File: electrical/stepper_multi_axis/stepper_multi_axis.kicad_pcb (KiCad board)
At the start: 4 copper layers, 152.4 x 69.8 mm, 71 parts, among them J1 Conn_01x04_Male, J10 Conn_01x02_Male, J11 Conn_01x01_Male, J12 Conn_01x01_Male, J13 Conn_01x06, J14 Conn_01x01_Male, J15 Conn_01x01_Male, J16 Conn_01x01_Male, J17 Conn_01x01_Male, J18 Conn_01x01_Male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

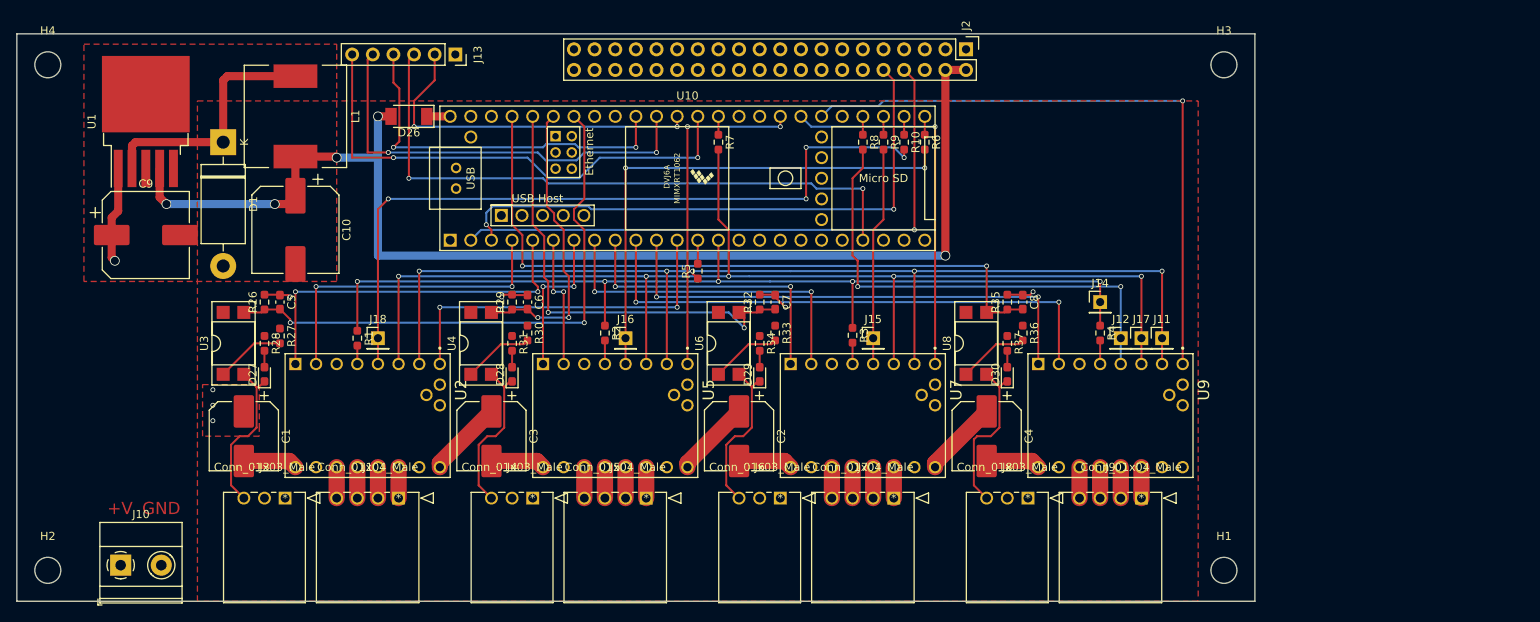
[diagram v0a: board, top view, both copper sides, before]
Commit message: added higher current drivers
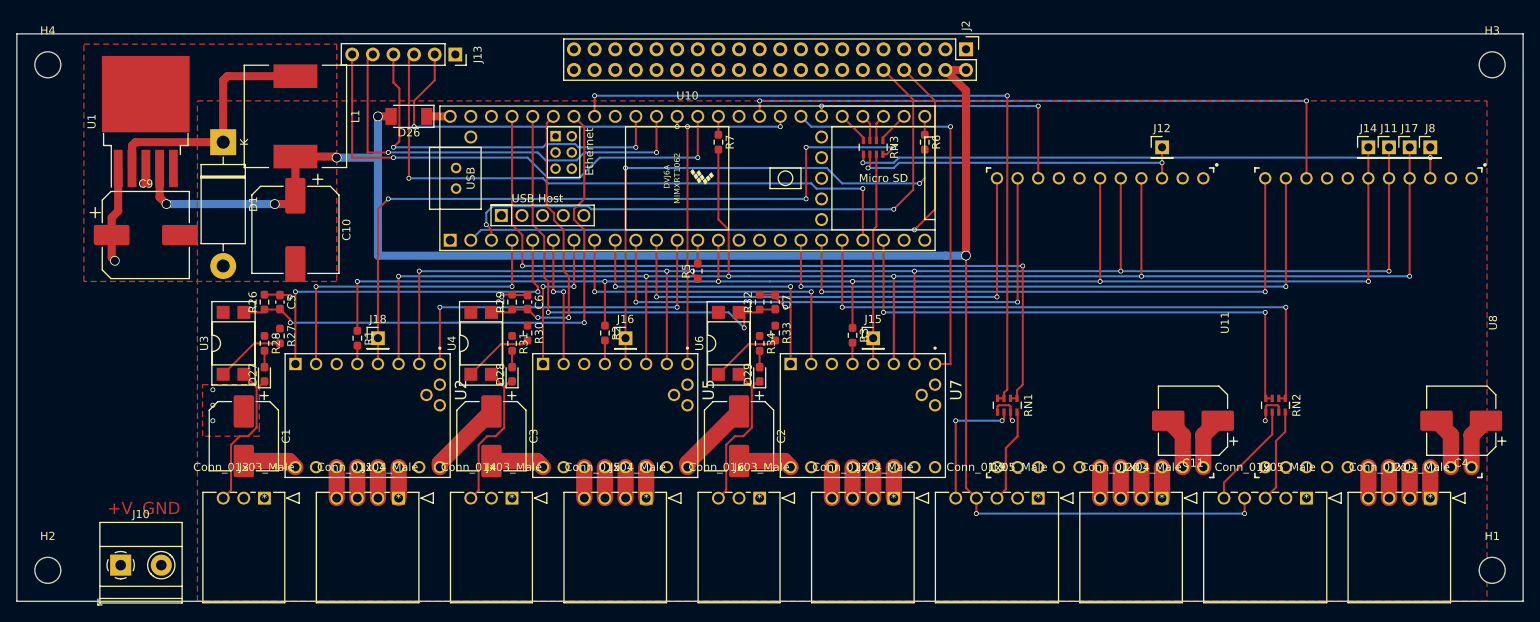
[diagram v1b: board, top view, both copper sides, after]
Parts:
- removed C8: 100nF, Capacitor_SMD:C_0603_1608Metric_Pad1.08x0.95mm_HandSolder
- removed D30: LED, LED_SMD:LED_0603_1608Metric_Pad1.05x0.95mm_HandSolder
- removed R10, R35, R36, R37, R4, R8, R9: 100, Resistor_SMD:R_0603_1608Metric_Pad0.98x0.95mm_HandSolder
- removed U9: TMC5160_SILENTSTEPSTICK, Trinamic:MODULE_TMC_SILENTSTEPSTICK
- added C11: 10uF, Capacitor_SMD:CP_Elec_8x6.7, F.Cu at (218.4, 128.9)
- added J19: Conn_01x05_Male, sl_connector:1719740105, F.Cu at (199.4, 138.4)
- added J20: Conn_01x04_Male, sl_connector:1719740104, F.Cu at (214.6, 138.4)
- added J21: Conn_01x04_Male, sl_connector:1719740104, F.Cu at (247.7, 138.4)
- added RN1: R_Pack04, Resistor_SMD:R_Array_Concave_4x0603, F.Cu at (195.6, 127.0)
- added RN2: R_Pack04, Resistor_SMD:R_Array_Concave_4x0603, F.Cu at (228.6, 127.0)
- added RN3: R_Pack04, Resistor_SMD:R_Array_Concave_4x0603, F.Cu at (179.1, 95.2)
- added U11: TMC5160-BOB, trinamic-footprints:22pin1,5x1,1-BOB, F.Cu at (207.0, 116.8)
- J8: value Conn_01x03_Male -> Conn_01x01_Male; footprint sl_connector:1719740103 -> Connector_PinHeader_2.54mm:PinHeader_1x01_P2.54mm_Vertical
- J9: value Conn_01x04_Male -> Conn_01x05_Male; footprint sl_connector:1719740104 -> sl_connector:1719740105
- U8: value LTV-817 -> TMC5160-BOB; footprint Package_DIP:DIP-4_W7.62mm_SMDSocket_SmallPads -> trinamic-footprints:22pin1,5x1,1-BOB
- moved J8 65.7 mm to (247.7, 95.2)
- moved C4 58.5 mm to (251.5, 128.9), turned to 180 degrees
- moved U8 48.3 mm to (240.0, 116.8), turned to 270 degrees
- moved J17 40.5 mm to (245.1, 95.2)
- moved J14 38.1 mm to (240.0, 95.2)
- moved J11 36.5 mm to (242.6, 95.2)
- moved H1 33.0 mm to (255.3, 147.3)
- moved H3 33.0 mm to (255.3, 85.1)
- moved J12 24.0 mm to (214.6, 95.2)
- moved J9 20.3 mm to (232.4, 138.4)
- moved J3 2.54 mm to (104.1, 138.4)
- moved J4 2.54 mm to (134.6, 138.4)
- moved J6 2.54 mm to (165.1, 138.4)
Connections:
- net /Stepper_Driver_X/CS renamed /CS_X
- net /sheet608DFF62/CS renamed /CS_Y
- net /sheet608FE262/CS renamed /CS_Z
- net /sheet608FE262/Limit renamed /LIM_Z
- J11 pad 1: /Stepper_Driver_X/SDI -> /MOSI
- J12 pad 1: /sheet608FE263/CS -> /CS_A
- J14 pad 1: /Stepper_Driver_X/SDO -> /MISO
- J17 pad 1: /Stepper_Driver_X/SCK -> /SCK
- J8 pad 1: +3V3 -> /CS_B
- J9 pad 1: Net-(J9-Pad1) -> GND
- J9 pad 4: Net-(J9-Pad4) -> +5V
- R1 pad 1: /Stepper_Driver_X/SDO -> /MISO
- R2 pad 1: /Stepper_Driver_X/SDO -> /MISO
- R3 pad 1: /Stepper_Driver_X/SDO -> /MISO
- R5 pad 1: /Stepper_Driver_X/SDI -> /MOSI
- R7 pad 2: /Stepper_Driver_X/SCK -> /SCK
- U10 pad 10: /RPi_GPIO/A_STEP -> /ST_A
- U10 pad 11: /RPi_GPIO/A_DIR -> /D_A
- U10 pad 14: /Stepper_Driver_X/SDO -> /MISO
- U10 pad 18: /RPi_GPIO/B_STEP -> /ST_B
- U10 pad 19: /RPi_GPIO/B_DIR -> /D_B
- U10 pad 20: /RPi_GPIO/B_LIMIT -> /ENCA_B
- U10 pad 22: Net-(U10-Pad22) -> /ENCB_B
- U10 pad 29: /RPi_GPIO/B_ENABLE -> Net-(RN3-Pad4)
- U10 pad 30: /RPi_GPIO/A_ENABLE -> /EN_A
- U10 pad 33: Net-(U10-Pad33) -> /EN_B
- U10 pad 41: /RPi_GPIO/COOLANT_FLOOD -> /ENCB_A
- U10 pad 45: /RPi_GPIO/A_LIMIT -> /ENCA_A
- U2 pad JP1_6: /Stepper_Driver_X/SCK -> /SCK
- U2 pad JP1_7: /Stepper_Driver_X/SDI -> /MOSI
- U5 pad JP1_6: /Stepper_Driver_X/SCK -> /SCK
- U5 pad JP1_7: /Stepper_Driver_X/SDI -> /MOSI
- U7 pad JP1_6: /Stepper_Driver_X/SCK -> /SCK
- U7 pad JP1_7: /Stepper_Driver_X/SDI -> /MOSI
- U8 pad 1: Net-(R36-Pad2) -> +3V3
- U8 pad 2: Net-(D30-Pad1) -> GND
- U8 pad 3: /RPi_GPIO/A_LIMIT -> /CS_B
- U8 pad 4: +3V3 -> /SCK
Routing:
- net /SCK: track 0.00 -> 200.9 mm, vias 0 -> 6
- net /MOSI: track 0.00 -> 181.5 mm, vias 0 -> 6
- net /MISO: track 0.00 -> 176.0 mm, vias 0 -> 6
- net /Stepper_Driver_X/SCK: track 150.7 -> 0.00 mm, vias 5 -> 0
- net /Stepper_Driver_X/SDI: track 138.3 -> 0.00 mm, vias 5 -> 0
- net /Stepper_Driver_X/SDO: track 119.2 -> 0.00 mm, vias 5 -> 0
- net /ENCA_A: track 0.00 -> 97.9 mm, vias 0 -> 2
- net /ENCB_A: track 0.00 -> 91.6 mm, vias 0 -> 2
- net /RPi_GPIO/A_LIMIT: track 86.4 -> 0.00 mm, vias 2 -> 0
- net /EN_B: track 0.00 -> 78.7 mm, vias 0 -> 2
- net /ST_B: track 0.00 -> 78.7 mm, vias 0 -> 2
- net /RPi_GPIO/A_ENABLE: track 77.6 -> 0.00 mm, vias 1 -> 0
- net /CS_B: track 0.00 -> 75.0 mm, vias 0 -> 2
- net /D_B: track 0.00 -> 74.9 mm, vias 0 -> 2
- net /ENCA_B: track 0.00 -> 74.9 mm, vias 0 -> 2
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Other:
- board size 152.4 x 69.8 mm -> 185.4 x 69.8 mm

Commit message: shipped things
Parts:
- added C12: 100nF, Capacitor_SMD:C_0603_1608Metric_Pad1.08x0.95mm_HandSolder, F.Cu at (74.9, 44.5)
- added C13: 100nF, Capacitor_SMD:C_0603_1608Metric_Pad1.08x0.95mm_HandSolder, F.Cu at (89.5, 40.5)
- added C8: 100nF, Capacitor_SMD:C_0603_1608Metric_Pad1.08x0.95mm_HandSolder, F.Cu at (67.8, 34.7)
- added D2: LED, Diode_SMD:D_0603_1608Metric_Pad1.05x0.95mm_HandSolder, F.Cu at (39.3, 79.7)
- added J22: Conn_01x02_Male, Connector_PinHeader_2.54mm:PinHeader_1x02_P2.54mm_Vertical, F.Cu at (52.5, 78.9)
- added J23: Conn_01x01, Connector_PinHeader_2.54mm:PinHeader_1x01_P2.54mm_Vertical, F.Cu at (61.5, 78.7)
- added J24: Conn_01x01, Connector_PinHeader_2.54mm:PinHeader_1x01_P2.54mm_Vertical, F.Cu at (58.0, 68.3)
- added J25: Conn_01x01, Connector_PinHeader_2.54mm:PinHeader_1x01_P2.54mm_Vertical, F.Cu at (65.5, 68.3)
- added J26: Conn_01x01, Connector_PinHeader_2.54mm:PinHeader_1x01_P2.54mm_Vertical, F.Cu at (55.8, 44.5)
- added J27: Conn_01x01, Connector_PinHeader_2.54mm:PinHeader_1x01_P2.54mm_Vertical, F.Cu at (57.8, 78.7)
- added J28: Conn_01x01, Connector_PinHeader_2.54mm:PinHeader_1x01_P2.54mm_Vertical, F.Cu at (46.4, 68.3)
- added J29: Conn_01x01, Connector_PinHeader_2.54mm:PinHeader_1x01_P2.54mm_Vertical, F.Cu at (50.4, 68.3)
- added J30: Conn_01x01, Connector_PinHeader_2.54mm:PinHeader_1x01_P2.54mm_Vertical, F.Cu at (54.1, 68.3)
- added J31: HDMI_A_1.4, HDMI:TE_1827059-3, F.Cu at (57.3, 29.5)
- added J32: USB_A, Connector_USB:USB_A_Molex_67643_Horizontal, F.Cu at (88.7, 36.4)
- added R4: 1k, Resistor_SMD:R_0603_1608Metric_Pad0.98x0.95mm_HandSolder, F.Cu at (43.0, 79.7)
- added R8: 2.2k, Resistor_SMD:R_0603_1608Metric_Pad0.98x0.95mm_HandSolder, F.Cu at (80.3, 41.2)
- added R9: 2.2k, Resistor_SMD:R_0603_1608Metric_Pad0.98x0.95mm_HandSolder, F.Cu at (80.3, 44.5)
- added U12: FSUSB42MUX, usbmux:SOP50P490X110-10N, F.Cu at (77.5, 43.3)
- added U9: Compute_Module_4_Connectors, RPi_Compute_Module_4:Raspberry-Pi-4-Compute-Module, F.Cu at (49.8, 56.7)
- D1: value 1N5822 -> D_Schottky; footprint Diode_THT:D_DO-201AD_P15.24mm_Horizontal -> Diode_SMD:D_SOD-128
- J13: value Conn_01x06 -> USB_B_Micro; footprint Connector_PinSocket_2.54mm:PinSocket_1x06_P2.54mm_Vertical -> Connector_USB:USB_Micro-B_Molex-105017-0001
- J2: value RPi_GPIO -> Conn_01x01; footprint RPi_Hat:Pin_Header_Straight_2x20 -> Connector_PinHeader_2.54mm:PinHeader_1x01_P2.54mm_Vertical
- RN1, RN2: value R_Pack04 -> R_1K_4
- RN3: value R_Pack04 -> R_100_4
- U3, U4, U6: footprint Package_DIP:DIP-4_W7.62mm_SMDSocket_SmallPads -> Package_DIP:DIP-4_W8.89mm_SMDSocket_LongPads
- moved H1 263.0 mm to (21.6, 26.7), turned to 180 degrees
- moved H3 233.7 mm to (21.6, 88.9), turned to 180 degrees
- moved H2 227.6 mm to (270.5, 26.7), turned to 180 degrees
- moved J10 211.2 mm to (261.5, 28.6), turned to 180 degrees
- moved H4 193.1 mm to (270.5, 88.9), turned to 180 degrees
- moved J21 179.0 mm to (100.3, 36.8), turned to 180 degrees
- moved C4 175.6 mm to (96.5, 46.4), turned to 0 degrees
- moved C9 172.9 mm to (258.4, 69.2), turned to 180 degrees
- moved J3 172.7 mm to (243.8, 36.8), turned to 180 degrees
- moved U1 169.1 mm to (258.4, 83.2), turned to 270 degrees
- moved C1 168.6 mm to (246.4, 44.5), turned to 90 degrees
- moved U3 160.2 mm to (247.7, 56.5), turned to 270 degrees
- moved D27 156.8 mm to (243.8, 52.1), turned to 270 degrees
- moved J9 154.8 mm to (115.6, 36.8), turned to 180 degrees
- moved R28 153.5 mm to (243.8, 55.9), turned to 90 degrees
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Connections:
- J13 pad 1: GND -> Net-(J13-Pad1)
- J13 pad 2: /RPi_GPIO/PROBE -> /Sheet614CFDB6/PROG-
- J13 pad 3: /RPi_GPIO/SAFETY_DOOR -> /Sheet614CFDB6/PROG+
- J13 pad 4: /RPi_GPIO/CYCLE_START -> Net-(J13-Pad4)
- J13 pad 5: /RPi_GPIO/FEED_HOLD -> GND
- J13 pad 6: /RPi_GPIO/CNC_RESET -> GND
- J2 pad 1: Net-(J2-Pad1) -> /Sheet613FBD85/USB_OTG
- U10 pad 2: /RPi_GPIO/PI_TX -> Net-(U10-Pad2)
- U10 pad 3: /RPi_GPIO/PI_RX -> Net-(U10-Pad3)
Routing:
- net +5V: track 220.9 -> 332.4 mm, vias 7 -> 8
- net /RPi_GPIO/SAFETY_DOOR: track 78.3 -> 0.00 mm, vias 2 -> 0
- net /RPi_GPIO/PI_TX: track 77.5 -> 0.00 mm, vias 1 -> 0
- net /RPi_GPIO/PI_RX: track 73.9 -> 0.00 mm, vias 2 -> 0
- net +3.3VA: track 0.00 -> 73.7 mm, vias 0 -> 1
- net /RPi_GPIO/CNC_RESET: track 62.4 -> 0.00 mm, vias 2 -> 0
- net /Sheet613FBD85/USB_OTG: track 0.00 -> 57.0 mm, vias 0 -> 2
- net /RPi_GPIO/FEED_HOLD: track 53.1 -> 0.00 mm, vias 2 -> 0
- net /RPi_GPIO/CYCLE_START: track 46.0 -> 0.00 mm, vias 2 -> 0
- net /RPi_GPIO/PROBE: track 43.6 -> 0.00 mm, vias 2 -> 0
- net /Sheet613FBD85/USB_N: track 0.00 -> 43.5 mm
- net /Sheet613FBD85/USB_P: track 0.00 -> 43.5 mm
- net GND: track 59.1 -> 81.6 mm, vias 5 -> 19
- net /Sheet613FBD85/HDMI0_HOTPLUG: track 0.00 -> 21.2 mm, vias 0 -> 2
- net /Sheet613FBD85/HDMI0_CEC: track 0.00 -> 17.3 mm, vias 0 -> 2
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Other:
- board size 185.4 x 69.8 mm -> 256.5 x 71.1 mm

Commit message: made some changes?
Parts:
- moved H1 95.6 mm to (3.81, -67.3)
- moved H2 95.6 mm to (252.7, -67.3)
- moved C1 94.4 mm to (228.6, -48.3)
- moved C10 94.4 mm to (225.4, -23.5)
- moved C12 94.4 mm to (57.1, -48.3)
- moved C13 94.4 mm to (71.8, -52.2)
- moved C2 94.4 mm to (167.6, -48.3)
- moved C3 94.4 mm to (198.1, -48.3)
- moved C5 94.4 mm to (224.2, -31.8)
- moved C6 94.4 mm to (193.7, -31.8)
- moved C7 94.4 mm to (163.2, -31.8)
- moved C8 94.4 mm to (50.0, -58.0)
- moved C9 94.4 mm to (240.7, -23.5)
- moved D1 94.4 mm to (233.0, -16.5)
- moved D2 94.4 mm to (21.5, -13.0)
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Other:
- outline, holes or cut-outs redrawn

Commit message: pre delete thru hole
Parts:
- removed H2, H3, H4: MountingHole, MountingHole:MountingHole_3.2mm_M3
- added C14: 100nF, Capacitor_SMD:C_0603_1608Metric_Pad1.08x0.95mm_HandSolder, F.Cu at (139.3, 45.3)
- added C15: 100nF, Capacitor_SMD:C_0603_1608Metric_Pad1.08x0.95mm_HandSolder, F.Cu at (120.9, 45.3)
- added C16: 10uF, Capacitor_SMD:C_0603_1608Metric_Pad1.08x0.95mm_HandSolder, F.Cu at (158.2, 31.5)
- added C17: 10uF, Capacitor_SMD:C_0603_1608Metric_Pad1.08x0.95mm_HandSolder, F.Cu at (162.2, 31.4)
- added C18: 10uF, Capacitor_SMD:C_0603_1608Metric_Pad1.08x0.95mm_HandSolder, F.Cu at (167.5, 40.3)
- added C19: 100nF, Capacitor_SMD:C_0603_1608Metric_Pad1.08x0.95mm_HandSolder, F.Cu at (179.3, 38.4)
- added J33: USB_A, Connector_USB:USB_A_Molex_67643_Horizontal, F.Cu at (145.0, 46.6)
- added J34: USB_A, Connector_USB:USB_A_Molex_67643_Horizontal, F.Cu at (126.6, 46.6)
- added J35: MICROMOD-2222-C, SparkFun-MicroMod:M.2-CONNECTOR-E, F.Cu at (163.4, 20.6)
- added J36: Conn_01x02_Male, Connector_PinHeader_2.54mm:PinHeader_1x02_P2.54mm_Vertical, F.Cu at (177.3, 20.1)
- added J37: Conn_01x02_Male, Connector_PinHeader_2.54mm:PinHeader_1x02_P2.54mm_Vertical, F.Cu at (177.3, 23.6)
- added J39: USB_B_Micro, Connector_USB:USB_Micro-B_Molex-105017-0001, F.Cu at (180.0, 56.2)
- added R10: 2.7k, Resistor_SMD:R_0603_1608Metric_Pad0.98x0.95mm_HandSolder, F.Cu at (170.4, 40.9)
- added R11: 2.2k, Resistor_SMD:R_0603_1608Metric_Pad0.98x0.95mm_HandSolder, F.Cu at (178.1, 51.1)
- added R12: 2.2k, Resistor_SMD:R_0603_1608Metric_Pad0.98x0.95mm_HandSolder, F.Cu at (179.3, 36.4)
- added R13: 100, Resistor_SMD:R_0603_1608Metric_Pad0.98x0.95mm_HandSolder, F.Cu at (271.3, 0.51)
- added R14: 100, Resistor_SMD:R_0603_1608Metric_Pad0.98x0.95mm_HandSolder, F.Cu at (271.3, 3.02)
- added R15: 100, Resistor_SMD:R_0603_1608Metric_Pad0.98x0.95mm_HandSolder, F.Cu at (275.6, 0.51)
- added RN4: R_100_4, Resistor_SMD:R_Array_Concave_4x0603, F.Cu at (157.2, 14.0)
- added U13: FE1.1s, Package_SO:SSOP-28_3.9x9.9mm_P0.635mm, F.Cu at (163.8, 35.8)
- added U14: FSUSB42MUX, usbmux:SOP50P490X110-10N, F.Cu at (173.8, 35.8)
- added Y1: Crystal, Crystal:Crystal_HC50_Vertical, F.Cu at (153.9, 39.0)
- moved J13 182.1 mm to (189.4, 56.2), turned to 0 degrees
- moved H1 177.1 mm to (167.4, 0.32)
- moved R8 160.2 mm to (185.0, 51.7), turned to 180 degrees
- moved J2 154.0 mm to (181.6, 51.6), turned to 180 degrees
- moved J32 138.4 mm to (163.4, 46.6), turned to 0 degrees
- moved J31 137.1 mm to (111.9, 53.3), turned to 0 degrees
- moved U12 134.2 mm to (167.9, 30.1), turned to 0 degrees
- moved C12 130.8 mm to (162.8, 28.8), turned to 180 degrees
- moved C13 130.0 mm to (157.7, 45.3), turned to 180 degrees
- moved R9 123.0 mm to (158.4, 28.8), turned to 180 degrees
- moved C8 117.9 mm to (101.4, 48.1), turned to 270 degrees
- moved J26 111.1 mm to (113.4, 33.3), turned to 180 degrees
- moved D2 109.0 mm to (129.9, -1.95), turned to 0 degrees
- moved U9 104.4 mm to (119.4, 21.0), turned to 270 degrees
- moved R4 101.5 mm to (126.1, -1.95), turned to 180 degrees
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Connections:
- J32 pad 2: /Sheet614CFDB6/USB_A- -> /Sheet614CFDB6/1-
- J32 pad 3: /Sheet614CFDB6/USB_A+ -> /Sheet614CFDB6/1+
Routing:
- net /Sheet614CFDB6/3+: track 0.00 -> 39.8 mm
- net /Sheet614CFDB6/3-: track 0.00 -> 39.8 mm
- net +5V: track 332.4 -> 369.0 mm, vias 8 -> 9
- net +3.3VA: track 73.7 -> 42.8 mm, vias 1 -> 5
- net /Sheet614CFDB6/OVERRIDE-: track 0.00 -> 24.8 mm
- net /Sheet614CFDB6/OVERRIDE+: track 0.00 -> 24.1 mm
- net /Sheet614CFDB6/2-: track 0.00 -> 23.7 mm
- net /Sheet614CFDB6/2+: track 0.00 -> 23.7 mm
- net GND: track 81.6 -> 103.6 mm, vias 19 -> 31
- net Net-(R11-Pad2): track 0.00 -> 19.9 mm, vias 0 -> 2
- net /Sheet614CFDB6/PROG+: track 15.0 -> 34.8 mm
- net /Sheet614CFDB6/PROG-: track 15.0 -> 34.1 mm
- net Net-(C17-Pad2): track 0.00 -> 16.9 mm, vias 0 -> 2
- net /Sheet613FBD85/USB_OTG: track 57.0 -> 41.1 mm
- net Net-(C18-Pad2): track 0.00 -> 14.1 mm, vias 0 -> 2
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- added copper zone on In2.Cu, net +3.3VA
- removed copper zone on In1.Cu, net GND
- removed copper zone on In2.Cu, net VBUS
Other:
- board size 256.5 x 71.1 mm -> 15.4 x 8.4 mm

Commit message: trying new stuff
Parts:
- removed D26: D_Schottky, Diode_SMD:D_SOD-128
- removed R5, R6, R7: 100, Resistor_SMD:R_0603_1608Metric_Pad0.98x0.95mm_HandSolder
- removed RN3: R_100_4, Resistor_SMD:R_Array_Concave_4x0603
- removed U10: Teensy4.1, teensy:Teensy41
- moved C10 132.9 mm to (85.3, -3.05)
- moved D1 132.9 mm to (93.0, 3.94)
- moved C9 132.9 mm to (100.6, -3.05)
- moved L1 132.9 mm to (84.1, 9.02)
- moved U1 132.9 mm to (100.6, 10.9)
- moved J27 111.4 mm to (217.1, -36.3), turned to 0 degrees
- moved R15 68.3 mm to (207.5, 6.10), turned to 270 degrees
- moved R14 62.3 mm to (209.0, 6.10), turned to 90 degrees
- moved R13 61.0 mm to (210.6, 6.10), turned to 270 degrees
- moved C8 59.6 mm to (156.5, 25.3)
- moved RN4 56.6 mm to (207.9, -11.3)
- moved H1 55.5 mm to (218.1, -22.4)
- moved J35 55.5 mm to (214.1, -2.16)
- moved J36 55.5 mm to (228.0, -2.67)
- moved J37 55.5 mm to (228.0, 0.89)
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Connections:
- J35 pad 50: Net-(J35-Pad50) -> /sheet608DFF62/Limit
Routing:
- net /CS_A: track 42.1 -> 139.0 mm
- net /CS_B: track 75.0 -> 170.2 mm, vias 2 -> 3
- net +5V: track 369.0 -> 461.3 mm, vias 9 -> 13
- net /ENCB_B: track 67.3 -> 157.1 mm, vias 2 -> 6
- net /ENCA_B: track 74.9 -> 162.1 mm, vias 2 -> 6
- net /D_B: track 74.9 -> 158.8 mm, vias 2 -> 6
- net /ST_B: track 78.7 -> 152.3 mm, vias 2 -> 6
- net /MOSI: track 181.5 -> 242.7 mm, vias 6 -> 8
- net /D_A: track 63.5 -> 123.3 mm, vias 2 -> 6
- net /CS_X: track 91.1 -> 32.4 mm, vias 4 -> 2
- net /CS_Z: track 26.0 -> 83.8 mm, vias 0 -> 2
- net /EN_A: track 36.8 -> 93.3 mm
- net /EN_B: track 78.7 -> 132.3 mm
- net /sheet608DFF62/STEP: track 16.5 -> 66.7 mm, vias 2 -> 6
- net /ST_A: track 69.9 -> 119.4 mm
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- added copper zone on In1.Cu, net GND
- added copper zone on In2.Cu, net VBUS

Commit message: bunches of changes
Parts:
- moved C18 0.38 mm to (218.4, 21.6)
- moved R8 0.36 mm to (236.1, 32.8)
- moved C12 0.13 mm to (213.5, 9.78)
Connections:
- J3 pad 1: +3V3 -> +3.3VA
- J4 pad 1: +3V3 -> +3.3VA
- J6 pad 1: +3V3 -> +3.3VA
- R27 pad 1: +3V3 -> +3.3VA
- R28 pad 1: +3V3 -> +3.3VA
- R30 pad 1: +3V3 -> +3.3VA
- R31 pad 1: +3V3 -> +3.3VA
- R33 pad 1: +3V3 -> +3.3VA
- R34 pad 1: +3V3 -> +3.3VA
- U11 pad 1: +3V3 -> +3.3VA
- U2 pad JP2_7: +3V3 -> +3.3VA
- U3 pad 4: +3V3 -> +3.3VA
- U4 pad 4: +3V3 -> +3.3VA
- U5 pad JP2_7: +3V3 -> +3.3VA
- U6 pad 4: +3V3 -> +3.3VA
- U7 pad JP2_7: +3V3 -> +3.3VA
- U8 pad 1: +3V3 -> +3.3VA
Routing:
- net /Sheet613FBD85/USB_N: track 41.3 -> 42.1 mm
- net /Sheet614CFDB6/INT+: track 12.2 -> 12.9 mm
- net /Sheet614CFDB6/OVERRIDE+: track 24.1 -> 24.8 mm
- net /Sheet614CFDB6/USB_INTERNAL_N: track 16.7 -> 17.4 mm
- net /Sheet614CFDB6/PROG-: track 34.1 -> 34.7 mm
- net /Sheet613FBD85/USB_OTG: track 78.0 -> 78.5 mm
- added copper zone on F.Cu, net +3.3VA
- removed copper zone on F.Cu, net +3V3
